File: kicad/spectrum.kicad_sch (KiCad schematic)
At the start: 34 parts

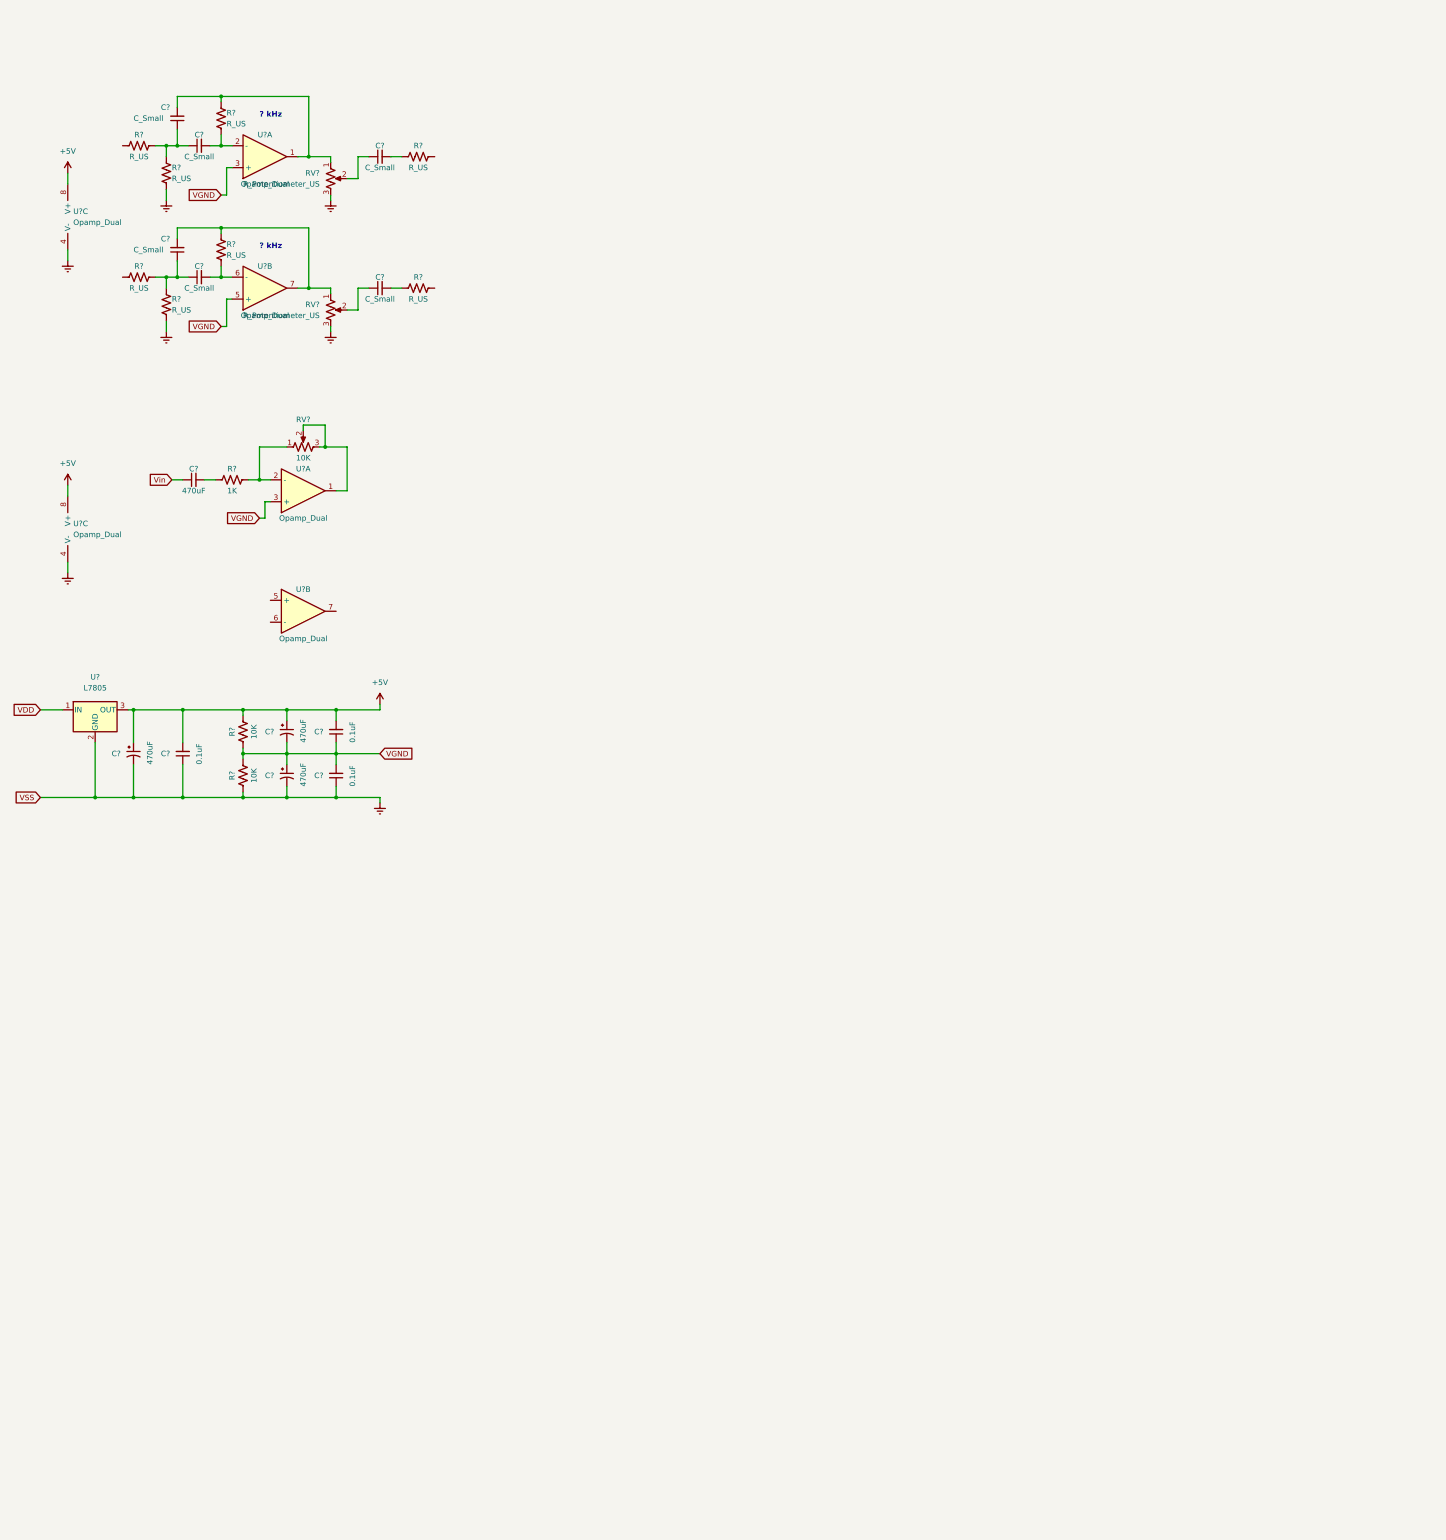
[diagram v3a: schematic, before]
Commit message: Band pass filter array
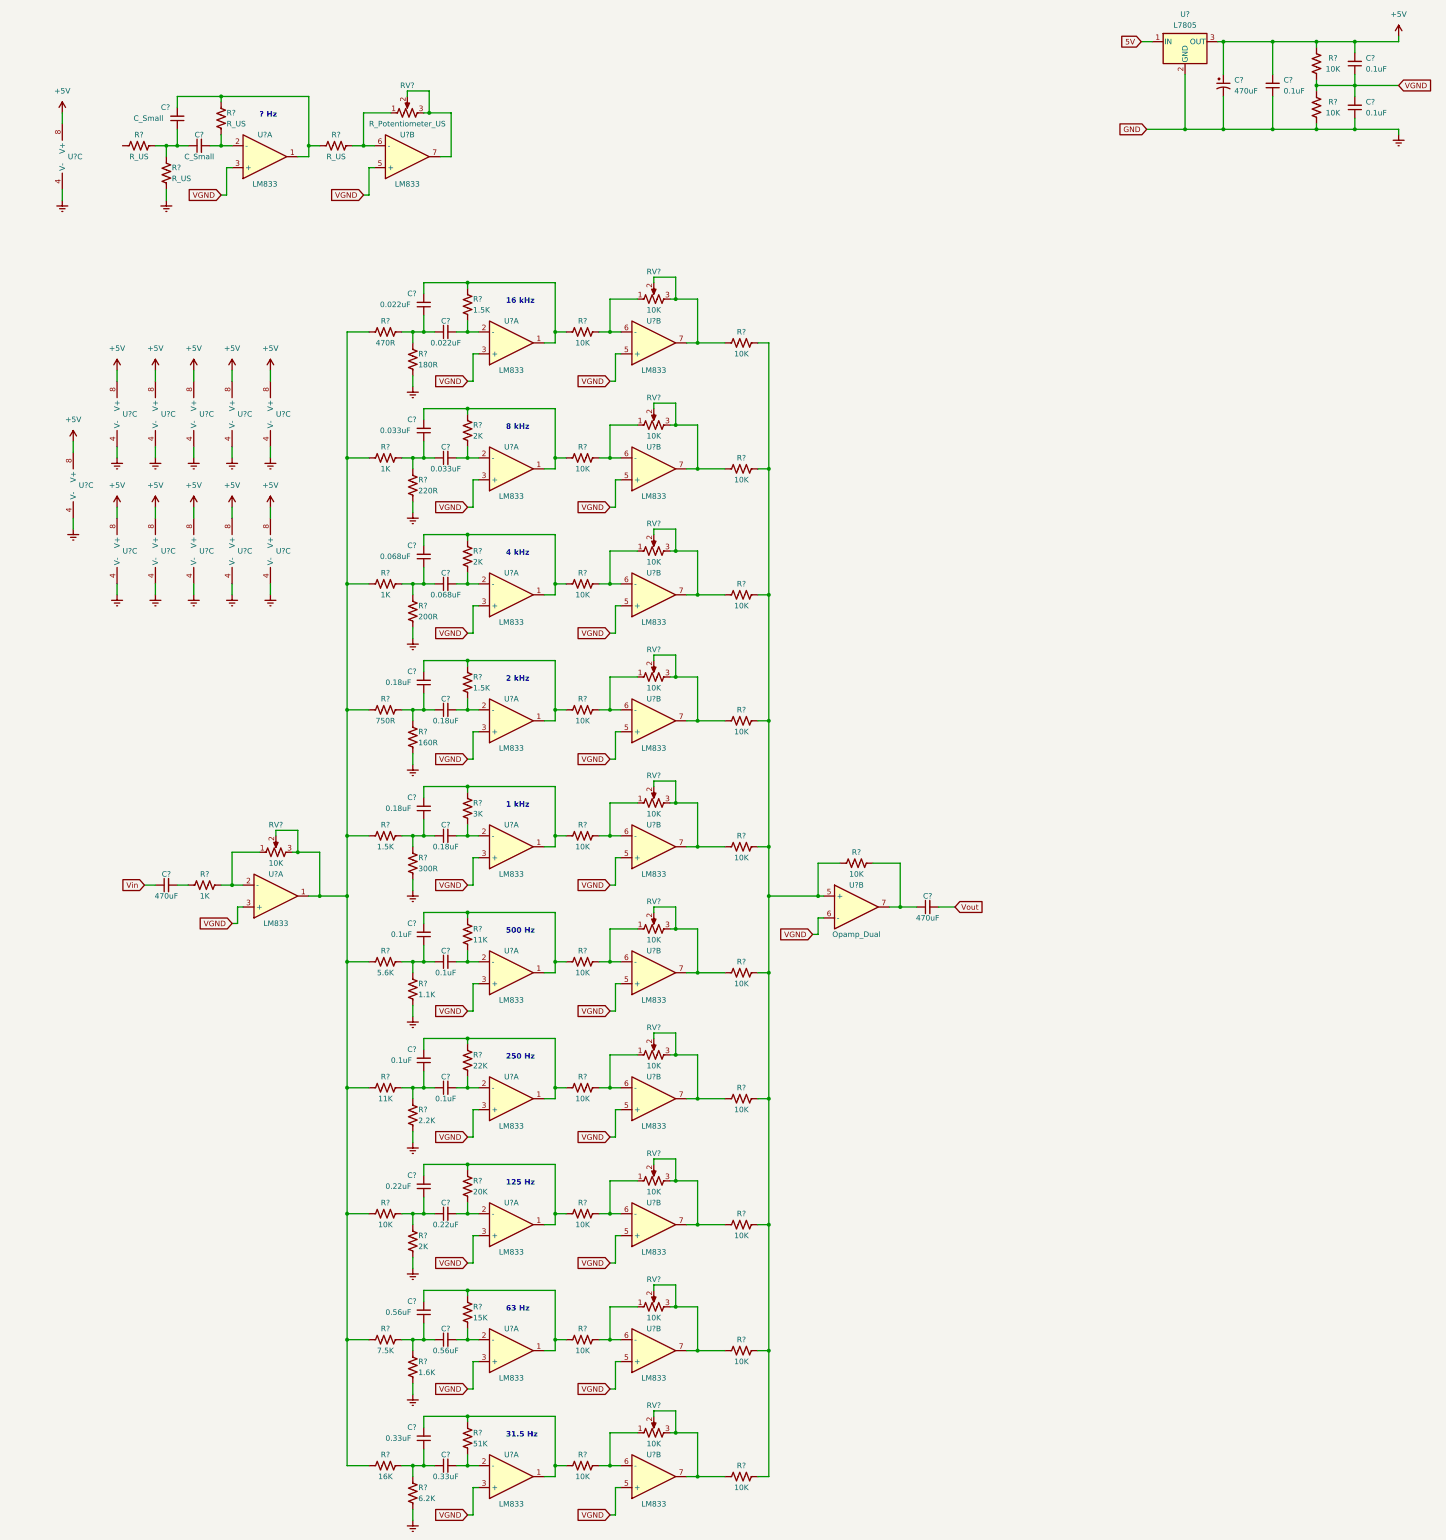
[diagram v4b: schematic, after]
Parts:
- removed C? (x4): C_Small, symbol Device:C_Small
- removed C? (x2): 470uF, symbol Device:C_Polarized_Small_US
- removed R? (x5): R_US, symbol Device:R_US
- removed RV? (x2): R_Potentiometer_US, symbol Device:R_Potentiometer_US
- removed U?: Opamp_Dual, symbol Device:Opamp_Dual
- added C? (x2): 0.033uF, symbol Device:C_Small
- added C? (x2): 0.33uF, symbol Device:C_Small
- added C? (x4): 0.1uF, symbol Device:C_Small
- added C? (x2): 0.022uF, symbol Device:C_Small
- added C? (x2): 0.068uF, symbol Device:C_Small
- added C? (x2): 0.56uF, symbol Device:C_Small
- added C?: 470uF, symbol Device:C_Small
- added C? (x2): 0.22uF, symbol Device:C_Small
- added C? (x4): 0.18uF, symbol Device:C_Small
- added R? (x22): 10K, symbol Device:R_US
- added R?: 20K, symbol Device:R_US
- added R? (x3): 2K, symbol Device:R_US
- added R? (x2): 11K, symbol Device:R_US
- added R?: 16K, symbol Device:R_US
- added R? (x3): 1.5K, symbol Device:R_US
- added R?: 2.2K, symbol Device:R_US
- added R?: 15K, symbol Device:R_US
- added R? (x2): 1K, symbol Device:R_US
- added R?: 1.1K, symbol Device:R_US
- added R?: 1.6K, symbol Device:R_US
- added R?: 5.6K, symbol Device:R_US
- added R?: 180R, symbol Device:R_US
- added R?: 6.2K, symbol Device:R_US
- added R?: 750R, symbol Device:R_US
- added R?: R_US, symbol Device:R_US
- added R?: 300R, symbol Device:R_US
- added R?: 22K, symbol Device:R_US
- added R?: 470R, symbol Device:R_US
- added R?: 51K, symbol Device:R_US
- added R?: 200R, symbol Device:R_US
- added R?: 3K, symbol Device:R_US
- added R?: 160R, symbol Device:R_US
- added R?: 220R, symbol Device:R_US
- added R?: 7.5K, symbol Device:R_US
- added RV? (x10): 10K, symbol Device:R_Potentiometer_US
- added RV?: R_Potentiometer_US, symbol Device:R_Potentiometer_US
- added U? (x31): LM833, symbol Device:Opamp_Dual
- U? (x4): value Opamp_Dual -> LM833
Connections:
- net +5V: now also U?.8 (V+), U?.8 (V+), U?.8 (V+), U?.8 (V+), U?.8 (V+), U?.8 (V+), U?.8 (V+), U?.8 (V+), U?.8 (V+), U?.8 (V+)
- net GNDREF: now also R?.2, R?.2, R?.2, R?.2, R?.2, R?.2, R?.2, R?.2, R?.2, R?.2, U?.4 (V-), U?.4 (V-), U?.4 (V-), U?.4 (V-), U?.4 (V-), U?.4 (V-), U?.4 (V-), U?.4 (V-), U?.4 (V-), U?.4 (V-)
- net VGND: now also U?.6 (-), U?.3 (+), U?.3 (+), U?.3 (+), U?.3 (+), U?.3 (+), U?.3 (+), U?.3 (+), U?.3 (+), U?.3 (+), U?.3 (+), U?.5 (+), U?.5 (+), U?.5 (+), U?.5 (+), U?.5 (+), U?.5 (+), U?.5 (+), U?.5 (+), U?.5 (+), U?.5 (+), U?.5 (+)
- net at C?.2, R?.1, U?.1: now also R?.2
- net at RV?.2, RV?.3, U?.1: now also R?.2, R?.2, R?.2, R?.2, R?.2, R?.2, R?.2, R?.2, R?.2, R?.2
- net at U?.5 (+): now also R?.1, R?.1, R?.1, R?.1, R?.1, R?.1, R?.1, R?.1, R?.1, R?.1, R?.2
- net at U?.7: now also C?.1, R?.1
- net VDD renamed 5V
- new net: R?.1, RV?.1, U?.6 (-) (x11)
- new net: R?.2, RV?.2, RV?.3, U?.7 (x10)
- new net: C?.1, C?.1, R?.1, R?.1 (x10)
- new net: C?.2, R?.1, R?.2, U?.1 (x10)
- new net: C?.2, R?.2, U?.2 (-) (x10)
- new net: RV?.2, RV?.3, U?.7
- new net Vout: C?.2
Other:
- note added: "1 kHz"
- note added: "125 Hz"
- note added: "16 kHz"
- note added: "2 kHz"
- note added: "250 Hz"
- note added: "31.5 Hz"
- note added: "4 kHz"
- note added: "500 Hz"
- note added: "63 Hz"
- note added: "8 kHz"
- note added: "? Hz"
- note removed: "? kHz"
- moved on the sheet: C?, R?, RV?, U?, U?A, U?B, U?C

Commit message: Left and right stereo filters
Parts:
- removed C? (x2): 470uF, symbol Device:C_Small
- removed C? (x2): C_Small, symbol Device:C_Small
- removed R? (x4): R_US, symbol Device:R_US
- removed RV?: R_Potentiometer_US, symbol Device:R_Potentiometer_US
- removed U? (x3): LM833, symbol Device:Opamp_Dual
- removed U?: Opamp_Dual, symbol Device:Opamp_Dual
- added C? (x6): 470uF, symbol Device:C_Polarized_Small_US
- added C? (x2): 0.56uF, symbol Device:C_Small
- added C? (x2): 0.033uF, symbol Device:C_Small
- added C? (x2): 0.22uF, symbol Device:C_Small
- added C? (x4): 0.18uF, symbol Device:C_Small
- added C? (x4): 0.1uF, symbol Device:C_Small
- added C? (x2): 0.068uF, symbol Device:C_Small
- added C? (x2): 0.33uF, symbol Device:C_Small
- added C? (x2): 0.022uF, symbol Device:C_Small
- added J?: Input, symbol Connector:AudioJack3_Ground
- added J?: Output, symbol Connector:AudioJack3_Ground
- added R?: 750R, symbol Device:R_US
- added R?: 5.6K, symbol Device:R_US
- added R? (x22): 10K, symbol Device:R_US
- added R?: 51K, symbol Device:R_US
- added R?: 16K, symbol Device:R_US
- added R?: 220R, symbol Device:R_US
- added R? (x2): 11K, symbol Device:R_US
- added R?: 7.5K, symbol Device:R_US
- added R?: 300R, symbol Device:R_US
- added R? (x3): 1K, symbol Device:R_US
- added R?: 470R, symbol Device:R_US
- added R?: 180R, symbol Device:R_US
- added R?: 22K, symbol Device:R_US
- added R?: 1.1K, symbol Device:R_US
- added R?: 3K, symbol Device:R_US
- added R?: 6.2K, symbol Device:R_US
- added R?: 160R, symbol Device:R_US
- added R? (x3): 1.5K, symbol Device:R_US
- added R? (x3): 2K, symbol Device:R_US
- added R?: 15K, symbol Device:R_US
- added R?: 2.2K, symbol Device:R_US
- added R?: 200R, symbol Device:R_US
- added R?: 1.6K, symbol Device:R_US
- added R?: 20K, symbol Device:R_US
- added RV? (x11): 10K, symbol Device:R_Potentiometer_US
- added U? (x34): LM833, symbol Device:Opamp_Dual
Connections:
- net +5V: now also C?.1, U?.8 (V+), U?.8 (V+), U?.8 (V+), U?.8 (V+), U?.8 (V+), U?.8 (V+), U?.8 (V+), U?.8 (V+), U?.8 (V+), U?.8 (V+), U?.8 (V+)
- net GNDREF: now also C?.2, J?.G, J?.G, J?.S, J?.S, R?.2, R?.2, R?.2, R?.2, R?.2, R?.2, R?.2, R?.2, R?.2, R?.2, U?.4 (V-), U?.4 (V-), U?.4 (V-), U?.4 (V-), U?.4 (V-), U?.4 (V-), U?.4 (V-), U?.4 (V-), U?.4 (V-), U?.4 (V-), U?.4 (V-)
- net VGND: now also C?.1, C?.2, U?.3 (+), U?.3 (+), U?.3 (+), U?.3 (+), U?.3 (+), U?.3 (+), U?.3 (+), U?.3 (+), U?.3 (+), U?.3 (+), U?.3 (+), U?.5 (+), U?.5 (+), U?.5 (+), U?.5 (+), U?.5 (+), U?.5 (+), U?.5 (+), U?.5 (+), U?.5 (+), U?.5 (+), U?.5 (+), U?.5 (+)
- net at R?.1, R?.1, R?.1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: now also U?.6 (-)
- net at R?.1: now also C?.1, U?.7
- net at R?.2: now also C?.2
- new net: C?.1, C?.1, R?.1, R?.1 (x10)
- new net: R?.2, R?.2, R?.2, R?.2, R?.2, R?.2, R?.2, R?.2, R?.2, R?.2, RV?.2, RV?.3, U?.1
- new net: R?.1, RV?.1, U?.6 (-) (x10)
- new net: C?.2, R?.1, R?.2, U?.1 (x10)
- new net: C?.2, R?.2, U?.2 (-) (x10)
- new net: R?.2, RV?.2, RV?.3, U?.7 (x10)
- new net: R?.1, R?.1, R?.1, R?.1, R?.1, R?.1, R?.1, R?.1, R?.1, R?.1, R?.2, U?.6 (-)
- new net: C?.1, R?.1, U?.7
- new net: C?.2, R?.2
- new net: R?.1, RV?.1, U?.2 (-)
- new net Vin_L: C?.1, J?.T
- new net Vin_R: C?.1, J?.R
- new net Vout_L: C?.2, J?.T
- new net Vout_R: C?.2, J?.R
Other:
- note removed: "? Hz"
- moved on the sheet: C?, R?, RV?, U?, U?A, U?B, U?C

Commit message: Footprint and symbol for Bourns PTL POT with LEDs
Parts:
- removed C? (x2): 0.56uF, symbol Device:C_Small
- removed C? (x2): 0.033uF, symbol Device:C_Small
- removed C? (x2): 0.22uF, symbol Device:C_Small
- removed C? (x4): 0.18uF, symbol Device:C_Small
- removed C? (x2): 470uF, symbol Device:C_Polarized_Small_US
- removed C? (x4): 0.1uF, symbol Device:C_Small
- removed C? (x2): 0.068uF, symbol Device:C_Small
- removed C? (x2): 0.33uF, symbol Device:C_Small
- removed C? (x2): 0.022uF, symbol Device:C_Small
- removed R?: 750R, symbol Device:R_US
- removed R?: 5.6K, symbol Device:R_US
- removed R? (x22): 10K, symbol Device:R_US
- removed R?: 51K, symbol Device:R_US
- removed R?: 16K, symbol Device:R_US
- removed R?: 220R, symbol Device:R_US
- removed R? (x2): 11K, symbol Device:R_US
- removed R?: 7.5K, symbol Device:R_US
- removed R?: 300R, symbol Device:R_US
- removed R? (x3): 1K, symbol Device:R_US
- removed R?: 470R, symbol Device:R_US
- removed R?: 180R, symbol Device:R_US
- removed R?: 22K, symbol Device:R_US
- removed R?: 1.1K, symbol Device:R_US
- removed R?: 3K, symbol Device:R_US
- removed R?: 6.2K, symbol Device:R_US
- removed R?: 160R, symbol Device:R_US
- removed R? (x3): 1.5K, symbol Device:R_US
- removed R? (x3): 2K, symbol Device:R_US
- removed R?: 15K, symbol Device:R_US
- removed R?: 2.2K, symbol Device:R_US
- removed R?: 200R, symbol Device:R_US
- removed R?: 1.6K, symbol Device:R_US
- removed R?: 20K, symbol Device:R_US
- removed RV? (x22): 10K, symbol Device:R_Potentiometer_US
- removed U? (x33): LM833, symbol Device:Opamp_Dual
- added C29, C50: 470uF, symbol Device:C_Polarized_Small_US
- added C30, C40: 0.022uF, symbol Device:C_Small
- added C31, C41: 0.033uF, symbol Device:C_Small
- added C32, C42: 0.068uF, symbol Device:C_Small
- added C33, C34, C43, C44: 0.18uF, symbol Device:C_Small
- added C35, C36, C45, C46: 0.1uF, symbol Device:C_Small
- added C37, C47: 0.22uF, symbol Device:C_Small
- added C38, C48: 0.56uF, symbol Device:C_Small
- added C39, C49: 0.33uF, symbol Device:C_Small
- added J1: Micro USB B, symbol Connector:USB_B_Micro
- added PTL1, PTL42: 100K, symbol bourns_ptl:Bourns_PTL
- added PTL10, PTL11, PTL2, PTL3, PTL32, PTL33, PTL34, PTL35, PTL36, PTL37, PTL38, PTL39, PTL4, PTL40, PTL41, PTL5, PTL6, PTL7, PTL8, PTL9: 10K, symbol bourns_ptl:Bourns_PTL
- added PTL12, PTL13, PTL14, PTL15, PTL16, PTL17, PTL18, PTL19, PTL20, PTL21, PTL22, PTL23, PTL24, PTL25, PTL26, PTL27, PTL28, PTL29, PTL30, PTL31: LED, symbol bourns_ptl:Bourns_PTL
- added R100: 3K, symbol Device:R_US
- added R101, R122: 11K, symbol Device:R_US
- added R102: 22K, symbol Device:R_US
- added R103: 20K, symbol Device:R_US
- added R104: 15K, symbol Device:R_US
- added R105: 51K, symbol Device:R_US
- added R106: 180R, symbol Device:R_US
- added R107: 220R, symbol Device:R_US
- added R108: 200R, symbol Device:R_US
- added R109: 160R, symbol Device:R_US
- added R110: 300R, symbol Device:R_US
- added R111: 1.1K, symbol Device:R_US
- added R112: 2.2K, symbol Device:R_US
- added R113, R97, R98: 2K, symbol Device:R_US
- added R114: 1.6K, symbol Device:R_US
- added R115: 6.2K, symbol Device:R_US
- added R116: 470R, symbol Device:R_US
- added R117, R118, R126, R52, R53, R55, R56, R57, R58, R59, R60, R61, R62, R65, R66, R67, R68, R69, R70, R71, R72, R74, R75: 1K, symbol Device:R_US
- added R119: 750R, symbol Device:R_US
- added R120, R96, R99: 1.5K, symbol Device:R_US
- added R121: 5.6K, symbol Device:R_US
- added R123, R73, R76, R77, R78, R79, R80, R81, R82, R83, R84, R85, R86, R87, R88, R89, R90, R91, R92, R93, R94, R95: 10K, symbol Device:R_US
- added R124: 7.5K, symbol Device:R_US
- added R125: 16K, symbol Device:R_US
- added SW1: POWER, symbol Switch:SW_SPST
- added SW2: RIGHT SOURCE, symbol Switch:SW_SPDT
- added SW3: LEFT SOURCE, symbol Switch:SW_SPDT
- added U12, U13, U14, U15, U16, U17, U18, U19, U20, U21, U22: LM833, symbol Device:Opamp_Dual
- gave numbers to parts that had none: 96
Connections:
- net +5V: now also R52.1, R53.1, R55.1, R56.1, R57.1, R58.1, R59.1, R60.1, R61.1, R62.1, R65.1, R66.1, R67.1, R68.1, R69.1, R70.1, R71.1, R72.1, R74.1, R75.1, U12.8 (V+), U13.8 (V+), U14.8 (V+), U15.8 (V+), U16.8 (V+), U17.8 (V+), U18.8 (V+), U19.8 (V+), U20.8 (V+), U21.8 (V+), U22.8 (V+)
- net GNDREF: now also J1.5 (GND), J1.6 (Shield), PTL12.5 (E), PTL13.5 (E), PTL14.5 (E), PTL15.5 (E), PTL16.5 (E), PTL17.5 (E), PTL18.5 (E), PTL19.5 (E), PTL20.5 (E), PTL21.5 (E), PTL22.5 (E), PTL23.5 (E), PTL24.5 (E), PTL25.5 (E), PTL26.5 (E), PTL27.5 (E), PTL28.5 (E), PTL29.5 (E), PTL30.5 (E), PTL31.5 (E), R106.2, R107.2, R108.2, R109.2, R110.2, R111.2, R112.2, R113.2, R114.2, R115.2, U12.4 (V-), U13.4 (V-), U14.4 (V-), U15.4 (V-), U16.4 (V-), U17.4 (V-), U18.4 (V-), U19.4 (V-), U20.4 (V-), U21.4 (V-), U22.4 (V-)
- net VGND: now also U12.3 (+), U12.5 (+), U13.3 (+), U13.5 (+), U14.3 (+), U14.5 (+), U15.3 (+), U15.5 (+), U16.3 (+), U16.5 (+), U17.3 (+), U17.5 (+), U18.3 (+), U18.5 (+), U19.3 (+), U19.5 (+), U20.3 (+), U20.5 (+), U21.3 (+), U21.5 (+), U22.3 (+), U22.5 (+)
- net Vin_L: now also C50.1, SW3.3 (C)
- net Vin_R: now also SW2.3 (C)
- net Vout_L: now also C29.2, SW3.1 (A); no longer J3.T
- net Vout_R: now also SW2.1 (A); no longer J3.R
- net at R33.1, U3.6 (-): now also PTL3.1
- net at R43.2, U3.7: now also PTL3.2, PTL3.3
- net at R46.2, U6.7: now also PTL6.2, PTL6.3
- net at R40.1, U10.6 (-): now also PTL10.1
- net at R50.2, U10.7: now also PTL10.2, PTL10.3
- net at R41.1, U11.6 (-): now also PTL11.1
- net at R51.2, U11.7: now also PTL11.2, PTL11.3
- net at R39.1, U9.6 (-): now also PTL9.1
- net at R49.2, U9.7: now also PTL9.2, PTL9.3
- net at R10.2, R11.2, R2.2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: now also PTL1.2, PTL1.3
- net at R48.2, U8.7: now also PTL8.2, PTL8.3
- net at R34.1, U4.6 (-): now also PTL4.1
- net at R44.2, U4.7: now also PTL4.2, PTL4.3
- net at R36.1, U6.6 (-): now also PTL6.1
- net at R38.1, U8.6 (-): now also PTL8.1
- net at R32.1, U2.6 (-): now also PTL2.1
- net at R35.1, U5.6 (-): now also PTL5.1
- net at R45.2, U5.7: now also PTL5.2, PTL5.3
- net at R1.1, U1.2 (-): now also PTL1.1
- net at R42.2, U2.7: now also PTL2.2, PTL2.3
- net at R37.1, U7.6 (-): now also PTL7.1
- net at R47.2, U7.7: now also PTL7.2, PTL7.3
- net 5V: no longer names the net of U23.1 (IN)
- net 5V: now also SW1.2 (B)
- new net: C38.1, C48.1, R114.1, R124.1
- new net: PTL42.2, PTL42.3, R116.2, R117.2, R118.2, R119.2, R120.2, R121.2, R122.2, R123.2, R124.2, R125.2, U12.1
- new net: R73.2, R76.1, R77.1, R78.1, R79.1, R80.1, R81.1, R82.1, R83.1, R84.1, R85.1, U12.6 (-)
- new net: PTL40.2, PTL40.3, R84.2, U21.7
- new net: PTL32.1, R86.1, U13.6 (-)
- new net: PTL32.2, PTL32.3, R76.2, U13.7
- new net: C40.2, R86.2, R96.1, U13.1
- new net: C30.2, R96.2, U13.2 (-)
- new net: PTL21.4 (B), R62.2
- new net: C45.2, R101.1, R91.2, U18.1
- new net: C35.2, R101.2, U18.2 (-)
- new net: C35.1, C45.1, R111.1, R121.1
- new net: C33.1, C43.1, R109.1, R119.1
- new net: C33.2, R99.2, U16.2 (-)
- new net: PTL41.1, R95.1, U22.6 (-)
- new net: C49.2, R105.1, R95.2, U22.1
- new net: PTL14.4 (B), R55.2
- new net: PTL20.4 (B), R61.2
- new net: C39.1, C49.1, R115.1, R125.1
- new net: C37.1, C47.1, R113.1, R123.1
- new net: PTL41.2, PTL41.3, R85.2, U22.7
- new net: C39.2, R105.2, U22.2 (-)
- new net: PTL12.4 (B), R52.2
- new net: PTL42.1, R126.1, U12.2 (-)
- new net: C44.2, R100.1, R90.2, U17.1
- new net: C34.2, R100.2, U17.2 (-)
- new net: PTL27.4 (B), R70.2
- new net: PTL19.4 (B), R60.2
- new net: C32.1, C42.1, R108.1, R118.1
- new net: C42.2, R88.2, R98.1, U15.1
- new net: C46.2, R102.1, R92.2, U19.1
- new net: C36.2, R102.2, U19.2 (-)
- new net: PTL24.4 (B), R67.2
- new net: PTL22.4 (B), R65.2
- new net: C36.1, C46.1, R112.1, R122.1
- new net: PTL37.2, PTL37.3, R81.2, U18.7
- new net: PTL39.1, R93.1, U20.6 (-)
- new net: C47.2, R103.1, R93.2, U20.1
- new net: PTL30.4 (B), R74.2
- new net: PTL26.4 (B), R69.2
- new net: PTL23.4 (B), R66.2
- new net: PTL40.1, R94.1, U21.6 (-)
- new net: J1.1 (VBUS), SW1.1 (A)
- new net: C29.1, R73.1, U12.7
- new net: C37.2, R103.2, U20.2 (-)
- new net: C38.2, R104.2, U21.2 (-)
- new net: PTL17.4 (B), R58.2
- new net: PTL28.4 (B), R71.2
- new net: PTL37.1, R91.1, U18.6 (-)
- new net: C31.1, C41.1, R107.1, R117.1
- new net: C43.2, R89.2, R99.1, U16.1
- new net: J3.R, SW2.2 (B)
- new net: PTL34.2, PTL34.3, R78.2, U15.7
- new net: PTL35.2, PTL35.3, R79.2, U16.7
- new net: PTL38.1, R92.1, U19.6 (-)
- new net: PTL38.2, PTL38.3, R82.2, U19.7
- new net: PTL29.4 (B), R72.2
- new net: C30.1, C40.1, R106.1, R116.1
- new net: PTL35.1, R89.1, U16.6 (-)
- new net: PTL16.4 (B), R57.2
- new net: C34.1, C44.1, R110.1, R120.1
- new net: PTL39.2, PTL39.3, R83.2, U20.7
- new net: PTL31.4 (B), R75.2
- new net: C48.2, R104.1, R94.2, U21.1
- new net: PTL33.2, PTL33.3, R77.2, U14.7
- new net: C50.2, R126.2
- new net: PTL36.1, R90.1, U17.6 (-)
- new net: PTL36.2, PTL36.3, R80.2, U17.7
- new net: PTL34.1, R88.1, U15.6 (-)
- new net: PTL13.4 (B), R53.2
- new net: C41.2, R87.2, R97.1, U14.1
- new net: C31.2, R97.2, U14.2 (-)
- new net: PTL33.1, R87.1, U14.6 (-)
- new net: J3.T, SW3.2 (B)
- new net: PTL25.4 (B), R68.2
- new net: C32.2, R98.2, U15.2 (-)
- new net: PTL18.4 (B), R59.2
- new net: PTL15.4 (B), R56.2
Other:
- moved on the sheet: C23, C24, C25, C26, C27, C28, J2, J3, R63, R64, U10C, U11C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
